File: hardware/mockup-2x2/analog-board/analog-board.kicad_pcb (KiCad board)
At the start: 4 copper layers, 100 x 62 mm, 138 parts, among them J1 12V, J2 COIL JOINT, J4 MCU, J5 PI ZERO, Q1 AO3401A, Q11 AO3400A, Q12 AO3400A, Q13 AO3400A, Q14 AO3400A, Q2 AO3400A, Q21 AO3401A, Q22 AO3401A, Q23 AO3401A, Q24 AO3401A, U1 TPS62150, U2 LP2985-5.0, U3 74HC4052, U4 AD8421, U5 OPA2810, U6 OPA2810, U7 ADuM1201, U8 74AHCT1G125

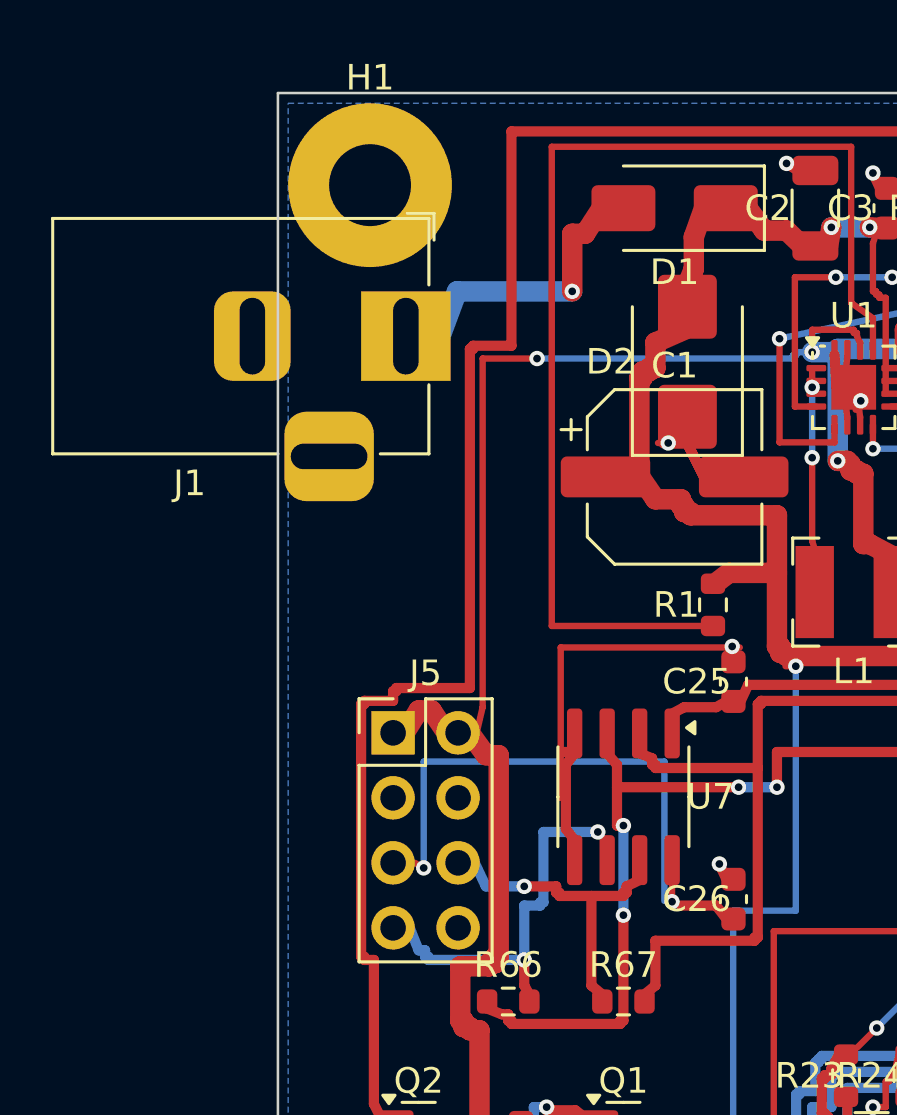
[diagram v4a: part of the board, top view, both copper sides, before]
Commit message: Carte analogique : le jack rentré dans le contour, et ses gerbers
La broche 2 du jack sortait de 1 mm à l'ouest depuis la première
génération. Le jack recule de 5 à 8 mm : ses trois pastilles sont
maintenant à 0,5 mm du bord, et son corps dépasse de 6 mm à l'ouest,
ce qui est la fonction d'un jack de panneau. Le routage se referme
sur ce placement, 558 pistes et 297 vias, zéro élément non connecté.

L'export a montré un second défaut : le fichier de carte déclarait
quatre couches cuivre. Le sérialiseur vient de la carte bobines, qui
en a quatre, et le générateur de la carte analogique ne disait pas les
siennes ; un fabricant aurait facturé et gravé une carte quatre
couches, et l'archive portait deux couches internes vides.

D'où l'archive commitée : `analog-board-gerbers.zip`, produite par
tools/gerbers.py, deux couches, pours remplis (B.Cu passe de 3 à
301 ko), perçages PTH et NPTH séparés, fichier de tâche. L'export.sh
de la carte appelle désormais cet outil au lieu de sa propre liste de
couches, et tests/test_gerbers.py épingle la pile de l'archive contre
celle que le fichier de carte déclare.

Reste un défaut de placement, documenté : 49 chevauchements de
courtyard, dont trente-deux dans le motif de cellule, où les
résistances de polarisation touchent le courtyard de leur diode
double. Les empreintes ne se chevauchent pas, la carte reste
assemblable, et les corriger demanderait de réespacer les cellules.
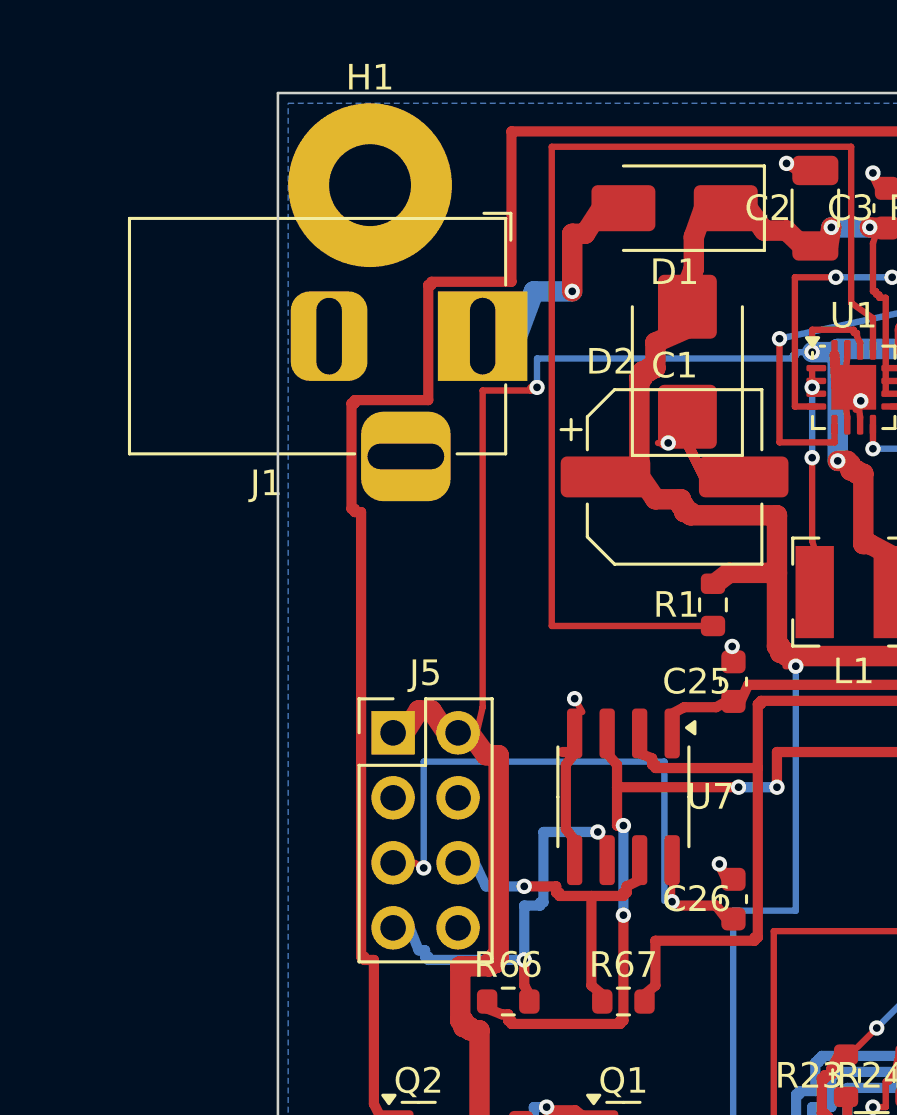
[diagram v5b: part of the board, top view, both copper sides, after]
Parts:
- moved J1 3.00 mm to (8.00, 9.50)
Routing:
- net GND: track 191.0 -> 178.7 mm, vias 46 -> 47
- net VIN_JACK: track 10.3 -> 7.31 mm
- net PULSE_EN: track 117.7 -> 118.4 mm
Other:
- copper layers 4 -> 2
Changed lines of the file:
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@@
   (layers
     (0 "F.Cu" signal)
-    (1 "In1.Cu" signal)
-    (2 "In2.Cu" signal)
     (31 "B.Cu" signal)
     (32 "B.Adhes" user "B.Adhesive")
@@
   (footprint "Connector_BarrelJack:BarrelJack_Horizontal" (version 20211014) (generator pcbnew)
     (layer "F.Cu")
-    (at 5 9.5)
+    (at 8 9.5)
     (descr "DC Barrel Jack")
     (tags "Power Jack")
@@
   (segment (start 20.875 14.25) (end 20.875 17.5) (width 0.25) (layer "F.Cu") (net 4))
   (segment (start 20.875 17.5) (end 20.975 17.825) (width 0.25) (layer "F.Cu") (net 4))
+  (segment (start 12.65 4.5) (end 12 5.5) (width 0.8) (layer "F.Cu") (net 1))
+  (segment (start 12 5.5) (end 11.5 5.5) (width 0.8) (layer "F.Cu") (net 1))
+  (segment (start 11.5 5.5) (end 11.5 7.75) (width 0.8) (layer "F.Cu") (net 1))
+  (segment (start 11.5 7.75) (end 10 7.75) (width 0.8) (layer "B.Cu") (net 1))
+  (segment (start 10 7.75) (end 9.35 9.5) (width 0.8) (layer "B.Cu") (net 1))
   (segment (start 14.1 41) (end 14 41.5) (width 0.8) (layer "F.Cu") (net 17))
   (segment (start 14 41.5) (end 14 42.5) (width 0.8) (layer "F.Cu") (net 17))
@@
   (segment (start 40.375 10.375) (end 40.25 10.375) (width 0.8) (layer "F.Cu") (net 11))
   (segment (start 40.25 10.375) (end 39.675 10.775) (width 0.8) (layer "F.Cu") (net 11))
-  (segment (start 12.65 4.5) (end 12 5.5) (width 0.8) (layer "F.Cu") (net 1))
-  (segment (start 12 5.5) (end 11.5 5.5) (width 0.8) (layer "F.Cu") (net 1))
-  (segment (start 11.5 5.5) (end 11.5 7.75) (width 0.8) (layer "F.Cu") (net 1))
-  (segment (start 11.5 7.75) (end 7 7.75) (width 0.8) (layer "B.Cu") (net 1))
-  (segment (start 7 7.75) (end 6.35 9.5) (width 0.8) (layer "B.Cu") (net 1))
   (segment (start 43.525 19.275) (end 42.875 18.875) (width 0.8) (layer "F.Cu") (net 13))
   (segment (start 42.875 18.875) (end 42.875 18.75) (width 0.8) (layer "F.Cu") (net 13))
@@
   (segment (start 20.125 10.25) (end 20.125 10.375) (width 0.25) (layer "B.Cu") (net 10))
   (segment (start 20.125 10.375) (end 10.125 10.375) (width 0.25) (layer "B.Cu") (net 10))
-  (segment (start 10.125 10.375) (end 8 10.375) (width 0.25) (layer "F.Cu") (net 10))
-  (segment (start 8 10.375) (end 8 24) (width 0.25) (layer "F.Cu") (net 10))
+  (segment (start 10.125 10.375) (end 10.125 11.5) (width 0.25) (layer "B.Cu") (net 10))
+  (segment (start 10.125 11.5) (end 9.875 11.5) (width 0.25) (layer "F.Cu") (net 10))
+  (segment (start 9.875 11.5) (end 9.875 11.625) (width 0.25) (layer "F.Cu") (net 10))
+  (segment (start 9.875 11.625) (end 8 11.625) (width 0.25) (layer "F.Cu") (net 10))
+  (segment (start 8 11.625) (end 8 24) (width 0.25) (layer "F.Cu") (net 10))
   (segment (start 8 24) (end 7.765 25) (width 0.25) (layer "F.Cu") (net 10))
   (segment (start 24.025 18.1) (end 23.125 17.625) (width 0.8) (layer "F.Cu") (net 10))
@@
   (segment (start 40.75 1.5) (end 39.25 1.5) (width 0.4) (layer "B.Cu") (net 18))
   (segment (start 39.25 1.5) (end 9.125 1.5) (width 0.4) (layer "F.Cu") (net 18))
-  (segment (start 9.125 1.5) (end 9.125 9.875) (width 0.4) (layer "F.Cu") (net 18))
-  (segment (start 9.125 9.875) (end 7.625 9.875) (width 0.4) (layer "F.Cu") (net 18))
-  (segment (start 7.625 9.875) (end 7.625 10) (width 0.4) (layer "F.Cu") (net 18))
-  (segment (start 7.625 10) (end 7.5 10) (width 0.4) (layer "F.Cu") (net 18))
-  (segment (start 7.5 10) (end 7.5 23.25) (width 0.4) (layer "F.Cu") (net 18))
-  (segment (start 7.5 23.25) (end 4.625 23.25) (width 0.4) (layer "F.Cu") (net 18))
-  (segment (start 4.625 23.25) (end 4.625 23.375) (width 0.4) (layer "F.Cu") (net 18))
-  (segment (start 4.625 23.375) (end 4.5 23.375) (width 0.4) (layer "F.Cu") (net 18))
-  (segment (start 4.5 23.375) (end 4.5 23.75) (width 0.4) (layer "F.Cu") (net 18))
-  (segment (start 4.5 23.75) (end 3.375 23.75) (width 0.4) (layer "F.Cu") (net 18))
-  (segment (start 3.375 23.75) (end 3.375 23.875) (width 0.4) (layer "F.Cu") (net 18))
-  (segment (start 3.375 23.875) (end 3.25 23.875) (width 0.4) (layer "F.Cu") (net 18))
-  (segment (start 3.25 23.875) (end 3.25 33.75) (width 0.4) (layer "F.Cu") (net 18))
+  (segment (start 9.125 1.5) (end 9.125 7.375) (width 0.4) (layer "F.Cu") (net 18))
+  (segment (start 9.125 7.375) (end 6 7.375) (width 0.4) (layer "F.Cu") (net 18))
+  (segment (start 6 7.375) (end 6 7.5) (width 0.4) (layer "F.Cu") (net 18))
+  (segment (start 6 7.5) (end 5.875 7.5) (width 0.4) (layer "F.Cu") (net 18))
+  (segment (start 5.875 7.5) (end 5.875 12) (width 0.4) (layer "F.Cu") (net 18))
+  (segment (start 5.875 12) (end 3 12) (width 0.4) (layer "F.Cu") (net 18))
+  (segment (start 3 12) (end 3 12.125) (width 0.4) (layer "F.Cu") (net 18))
+  (segment (start 3 12.125) (end 2.875 12.125) (width 0.4) (layer "F.Cu") (net 18))
+  (segment (start 2.875 12.125) (end 2.875 16.25) (width 0.4) (layer "F.Cu") (net 18))
+  (segment (start 2.875 16.25) (end 3 16.25) (width 0.4) (layer "F.Cu") (net 18))
+  (segment (start 3 16.25) (end 3 16.375) (width 0.4) (layer "F.Cu") (net 18))
+  (segment (start 3 16.375) (end 3.25 16.375) (width 0.4) (layer "F.Cu") (net 18))
+  (segment (start 3.25 16.375) (end 3.25 33.75) (width 0.4) (layer "F.Cu") (net 18))
   (segment (start 3.25 33.75) (end 3.375 33.75) (width 0.4) (layer "F.Cu") (net 18))
   (segment (start 3.375 33.75) (end 3.375 33.875) (width 0.4) (layer "F.Cu") (net 18))
@@
   (segment (start 62.457789 21.302602) (end 62.457789 25.632729) (width 0.25) (layer "F.Cu") (net 2))
   (segment (start 62.457789 25.632729) (end 62.457789 25.632729) (width 0.25) (layer "B.Cu") (net 2))
-  (segment (start 18.047115 21.664116) (end 11.05 21.664116) (width 0.25) (layer "F.Cu") (net 2))
-  (segment (start 11.05 21.664116) (end 11.05 27.54) (width 0.25) (layer "F.Cu") (net 2))
+  (segment (start 11.894278 24.185297) (end 11.594278 23.665682) (width 0.25) (layer "F.Cu") (net 2))
+  (segment (start 11.594278 23.665682) (end 11.594278 23.665682) (width 0.25) (layer "B.Cu") (net 2))
   (segment (start 31.35 43) (end 31.35 41.5) (width 0.25) (layer "F.Cu") (net 2))
   (segment (start 31.35 41.5) (end 31.2 41.35) (width 0.25) (layer "F.Cu") (net 2))
@@
   (via (at 25.75 48.625) (size 0.6) (drill 0.3) (layers "F.Cu" "B.Cu") (net 3))
   (via (at 20.875 10.125) (size 0.6) (drill 0.3) (layers "F.Cu" "B.Cu") (net 10))
-  (via (at 10.125 10.375) (size 0.6) (drill 0.3) (layers "F.Cu" "B.Cu") (net 10))
+  (via (at 10.125 11.5) (size 0.6) (drill 0.3) (layers "F.Cu" "B.Cu") (net 10))
   (via (at 21.875 14.375) (size 0.6) (drill 0.3) (layers "F.Cu" "B.Cu") (net 10))
   (via (at 24.5 10) (size 0.6) (drill 0.3) (layers "F.Cu" "B.Cu") (net 10))
@@
   (via (at 55.65 28.605) (size 0.6) (drill 0.3) (layers "F.Cu" "B.Cu") (net 2))
   (via (at 62.457789 25.632729) (size 0.6) (drill 0.3) (layers "F.Cu" "B.Cu") (net 2))
+  (via (at 11.594278 23.665682) (size 0.6) (drill 0.3) (layers "F.Cu" "B.Cu") (net 2))
   (via (at 31.2 41.35) (size 0.6) (drill 0.3) (layers "F.Cu" "B.Cu") (net 2))
   (via (at 27.5 41.35) (size 0.6) (drill 0.3) (layers "F.Cu" "B.Cu") (net 2))

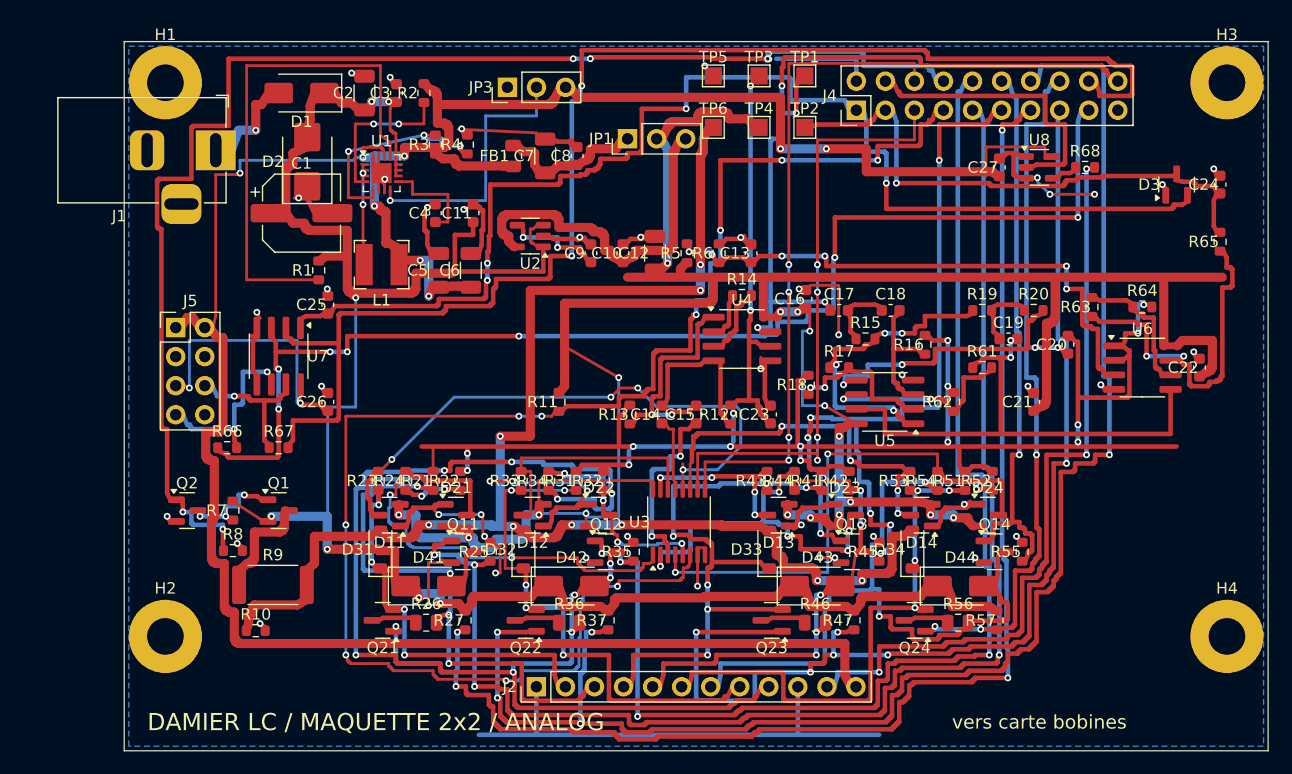
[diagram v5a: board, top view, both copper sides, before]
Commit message: Carte analogique : placement, courtyards et routage à zéro défaut
Les 49 chevauchements de courtyard sont corrigés dans le placement et
le routage a été rejoué dessus. Le build vérifie maintenant cette
famille lui même (tools/analoggen/yards.py) : il lit les courtyards des
empreintes, les pose, compte les paires qui se recouvrent, exactement
comme KiCad, et sort le nombre sur sa ligne d'état.

Le replacement a rouvert des liaisons, fermées par des routes
structurelles plutôt qu'une à une : la traversée de sa rangée par la
ligne B de chaque cellule, face avant, dans le canal de 0,86 mm entre
les deux rangées ; le contournement du coin sud-est, sans aucune
pastille, pour la ligne B de la cellule 4 ; la descente de sa rangée B
par la face arrière de la bande, où l'écrêteur et le FET, tous deux en
CMS, ne bloquent rien ; une épine de masse pour le tampon LED, coincé
sous le connecteur Nucleo entre vingt échappées. Le routeur joue un
tour de plus, chaque tour promouvant ce que le précédent a manqué, et
le labyrinthe dégrossit sa trame (0,1 puis 0,2 mm) quand la liaison
traverse la carte au lieu d'abandonner sur son plafond.

Le contrôle exact jugeait la garde au plancher de fabrication de
0,127 mm là où KiCad la juge à la valeur de la classe de nets, 0,15 :
il laissait donc passer une piste à 0,136 mm que le DRC comptait comme
une erreur. Le contrôle et la passe de retrait utilisent la valeur de
la classe de nets, la finition redessine ce qui est retiré, et les deux
comptes sont de nouveau d'accord.

État : 568 pistes, 288 vias, zéro liaison ouverte, zéro erreur au DRC
de KiCad toutes familles confondues, zéro chevauchement de courtyard.
Archive et empreinte regénérées.
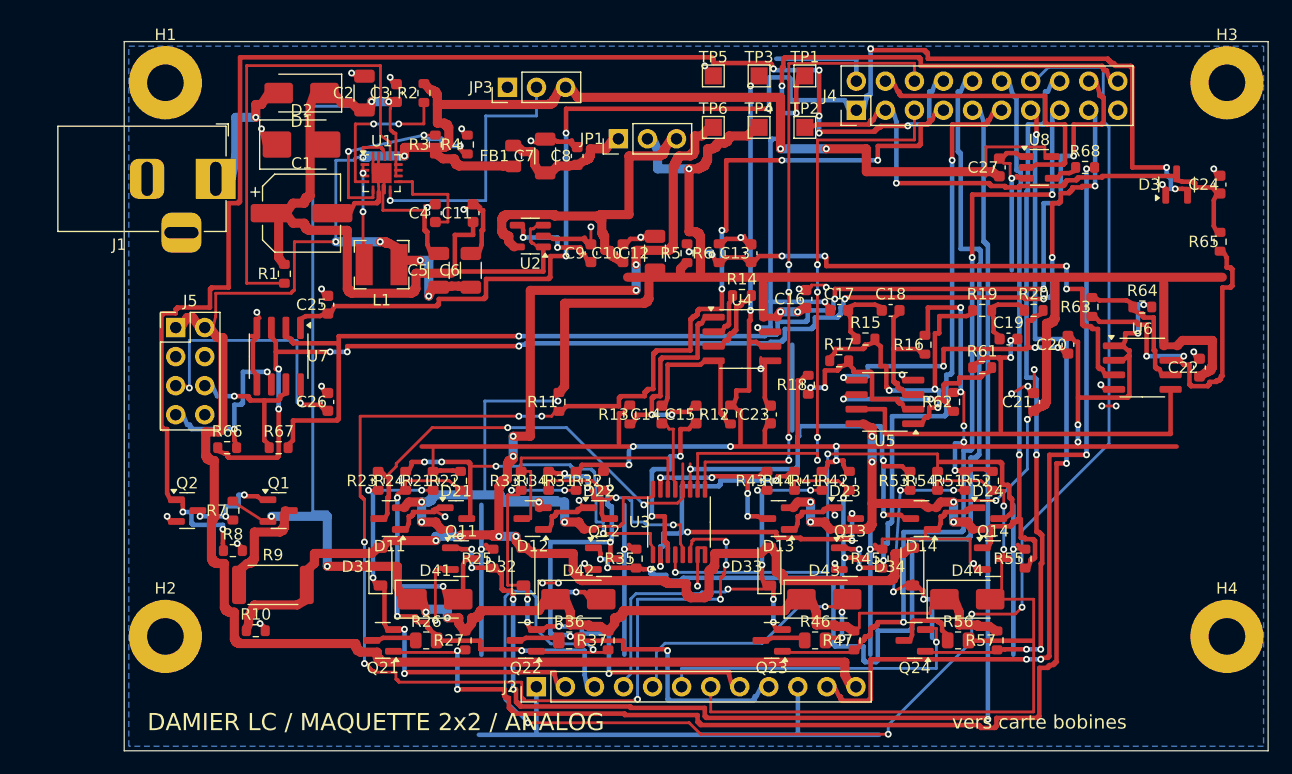
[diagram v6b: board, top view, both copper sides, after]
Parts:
- moved R1 3.01 mm to (14.0, 20.3)
- moved J1 2.50 mm to (8.00, 12.0)
- moved Q21 1.75 mm to (22.6, 52.4)
- moved Q22 1.75 mm to (35.1, 52.4)
- moved Q23 1.75 mm to (56.6, 52.4)
- moved Q24 1.75 mm to (69.1, 52.4)
- moved R27 1.75 mm to (29.8, 52.4)
- moved R37 1.75 mm to (42.3, 52.4)
- moved R47 1.75 mm to (63.8, 52.4)
- moved R57 1.75 mm to (76.3, 52.4)
- moved D2 1.58 mm to (15.5, 9.00), turned to 0 degrees
- moved R26 1.55 mm to (26.4, 52.4)
- moved R36 1.55 mm to (38.9, 52.4)
- moved R46 1.55 mm to (60.4, 52.4)
- moved R56 1.55 mm to (72.9, 52.4)
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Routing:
- net GND: track 178.7 -> 242.0 mm, vias 47 -> 45
- net C2_B: track 109.3 -> 55.1 mm, vias 10 -> 5
- net DAMP3_N: track 101.3 -> 70.3 mm, vias 6 -> 3
- net VIN: track 164.1 -> 192.1 mm, vias 7 -> 6
- net DRIVE3: track 72.6 -> 53.9 mm, vias 7 -> 4
- net C3_A: track 53.0 -> 37.4 mm
- net M1_A: track 50.8 -> 37.6 mm, vias 4 -> 2
- net MCU_RX: track 121.3 -> 108.3 mm, vias 2 -> 4
- net DRIVE2: track 108.7 -> 96.2 mm, vias 4 -> 3
- net 5VA: track 231.5 -> 219.6 mm, vias 17 -> 16
- net MUX_INH: track 140.6 -> 150.5 mm, vias 10 -> 12
- net C1_B: track 57.2 -> 47.7 mm, vias 5 -> 4
- net 3V3_NUCLEO: track 107.7 -> 116.3 mm, vias 4 -> 6
- net DRIVE1: track 122.7 -> 114.2 mm, vias 4 -> 5
- net M1_B: track 42.4 -> 34.1 mm, vias 2 -> 4
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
